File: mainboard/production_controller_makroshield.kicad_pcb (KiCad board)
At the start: 2 copper layers, 165.1 x 202.5 mm, 96 parts, among them J1 CON_TERM_BLK_1X2_TB008A-508-0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, J10 CON_CONNAXIO_MOTOR_DRIVER, J11 CON_CONNAXIO_MOTOR_DRIVER, J12 CON_CONNAXIO_MOTOR_DRIVER, J13 CON_CONNAXIO_MOTOR_DRIVER, J14 CON_CONNAXIO_MOTOR_DRIVER, J15 CON_CONNAXIO_MOTOR_DRIVER, J16 CON_CONNAXIO_MOTOR_DRIVER, J17 CON_CONNAXIO_MOTOR_DRIVER, J18 CON_CONNAXIO_MOTOR_DRIVER, J19 CON_CONNAXIO_MOTOR_DRIVER, J2 CON_TERM_BLK_1X2_TB008A-508-0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, J20 CON_CONNAXIO_MOTOR_DRIVER, J3 CON_HDR_MIKROBUS_ADDON_TH, J4 CON_TERM_BLK_1X2_TB008A-508-0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, J5 CON_HDR_MIKROBUS_SOCKET_TH, J6 CON_CONNAXIO_MOTOR_DRIVER, J7 CON_CONNAXIO_MOTOR_DRIVER, J8 CON_CONNAXIO_MOTOR_DRIVER, J9 CON_CONNAXIO_MOTOR_DRIVER, Q1 TRX_PMOS_AOD4189, Q2 TRX_NPN_MMBT3904-TP, U1 IO_EXP_PI4IOE5V6416ZDEX, U2 IO_EXP_PI4IOE5V6416ZDEX, U3 SUN_CUR_ACS711KEXLT-31AB-T, U4 ADC_NAU7802SGI

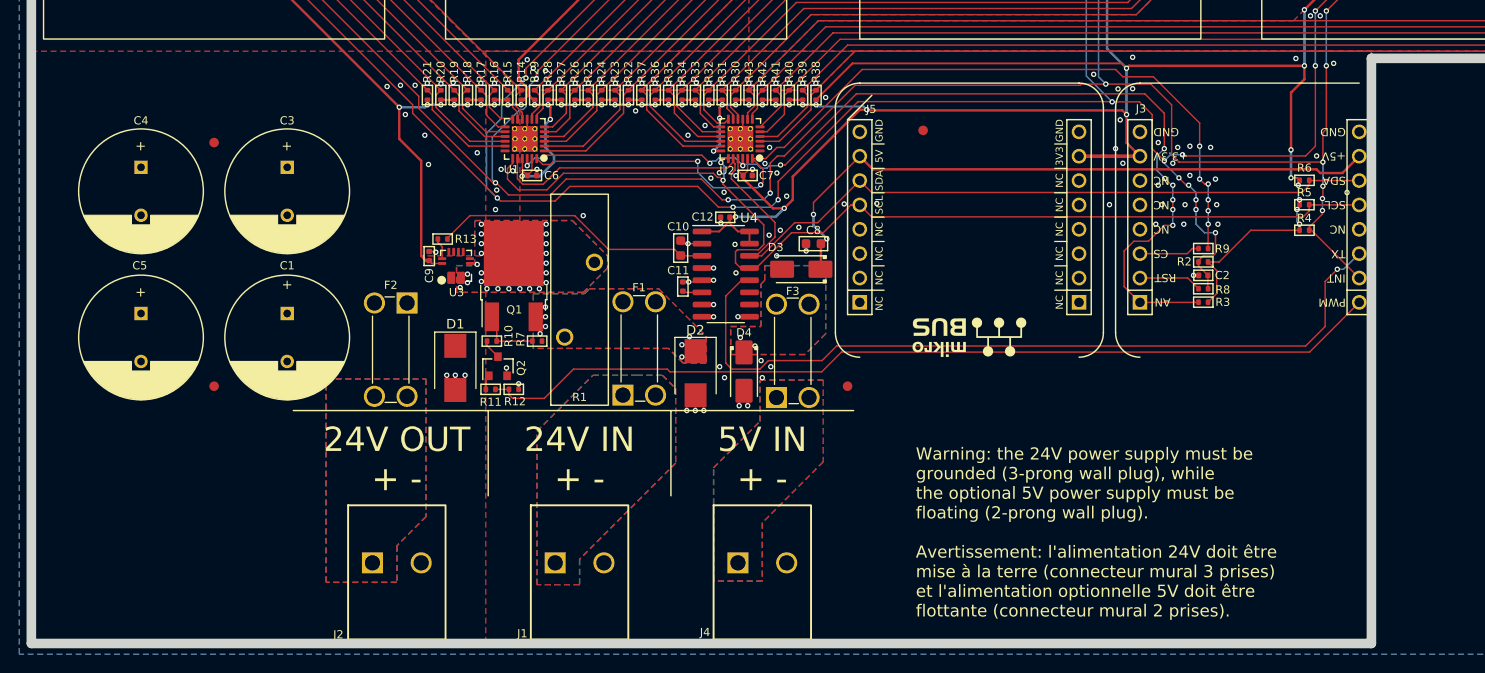
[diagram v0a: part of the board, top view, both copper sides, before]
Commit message: Add LEDs, fix NMOS, Add logos and infos on PCBs.
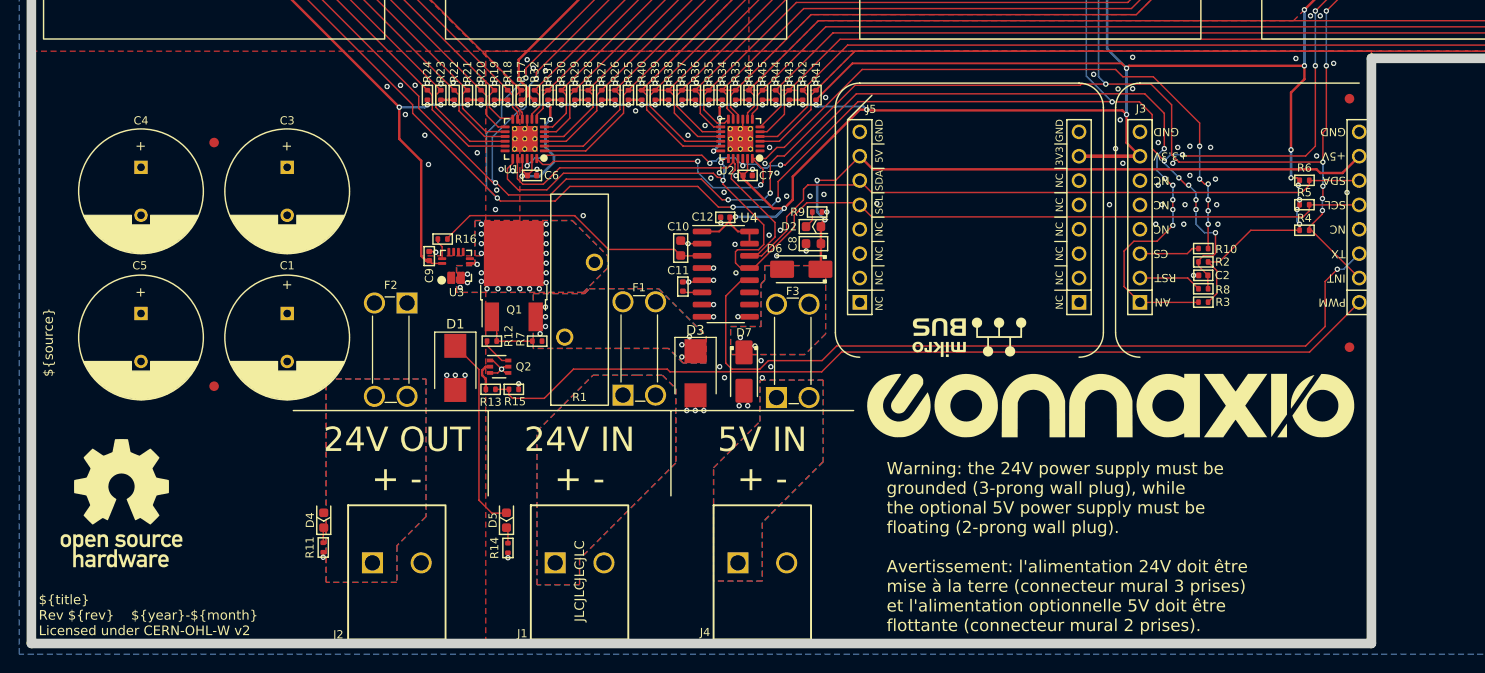
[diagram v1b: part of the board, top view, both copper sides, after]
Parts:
- added D2: DIO_LED_GREEN_150060GS75000, connaxio-diodes:LED_0603_1608M, F.Cu at (159.1, 193.7)
- added D4: DIO_LED_GREEN_150060GS75000, connaxio-diodes:LED_0603_1608M, F.Cu at (108.0, 224.3)
- added D5: DIO_LED_GREEN_150060GS75000, connaxio-diodes:LED_0603_1608M, F.Cu at (127.1, 224.3)
- added G***: LOGO, LOGO, F.Cu at (190.1, 212.4)
- added G***: LOGO, LOGO, F.Cu at (87.0, 222.6)
- added R11: RES_5.10KΩ_1%_0402, connaxio-resistors:RES_0402_1005M, F.Cu at (108.0, 227.2)
- added R14: RES_5.10KΩ_1%_0402, connaxio-resistors:RES_0402_1005M, F.Cu at (127.3, 227.2)
- added R9: RES_1.00KΩ_1%_0402, connaxio-resistors:RES_0402_1005M, F.Cu at (159.5, 192.2)
- Q2: value TRX_NPN_MMBT3904-TP -> TRX_2NPN_BC846S,115; footprint connaxio-sop:SOT-23-3 -> connaxio-sop:SOT-363_SC-70-6
- moved F6 52.5 mm to (215.0, 206.3)
- moved F5 44.6 mm to (215.0, 180.4)
- moved Q2 0.14 mm to (126.3, 208.3), turned to 0 degrees
- renumbered D2 to D3, D3 to D6, D4 to D7, R9 to R10, R10 to R12, R11 to R13, R12 to R15, R13 to R16, R14 to R17, R15 to R18, R16 to R19, R17 to R20, R18 to R21, R19 to R22, R20 to R23, R21 to R24, R22 to R25, R23 to R26, R24 to R27, R25 to R28, R26 to R29, R27 to R30, R28 to R31, R29 to R32, R30 to R33, R31 to R34, R32 to R35, R33 to R36, R34 to R37, R35 to R38, R36 to R39, R37 to R40, R38 to R41, R39 to R42, R40 to R43, R41 to R44, R42 to R45, R43 to R46
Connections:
- Q2 pad 1: Net-(Q2-Pad1) -> GND
- Q2 pad 2: GND -> Net-(R13-Pad2)
- Q2 pad 3: Net-(Q2-Pad3) -> GND
- R12 pad 2: Net-(Q2-Pad3) -> Net-(R12-Pad2)
- R13 pad 2: Net-(Q2-Pad1) -> Net-(R13-Pad2)
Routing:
- net +24VDC: track 0.00 -> 20.6 mm
- net GND: track 24.0 -> 28.8 mm, vias 216 -> 219
- net Net-(R12-Pad2): track 0.00 -> 3.33 mm
- net Net-(R13-Pad2): track 0.00 -> 3.14 mm
- net +5V: track 68.2 -> 70.6 mm
- net Net-(Q2-Pad3): track 2.08 -> 0.00 mm
- net Net-(D2-Pad1): track 0.00 -> 1.80 mm
- net Net-(D5-Pad1): track 0.00 -> 1.65 mm
- net Net-(D4-Pad1): track 0.00 -> 1.59 mm
- net Net-(Q2-Pad1): track 1.54 -> 0.00 mm
- net /I2C_SDA: track 107.2 -> 108.7 mm
- net /I2C_SCL: track 111.6 -> 112.5 mm
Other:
- board text added: "${source}"
- board text added: "${title} Rev ${rev} ${year}-${month} Licensed under CERN-OHL-W v2"
- board text added: "JLCJLCJLCJLC"

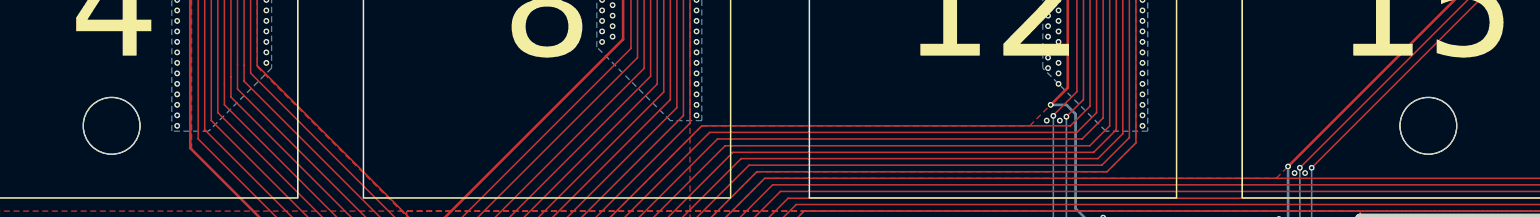
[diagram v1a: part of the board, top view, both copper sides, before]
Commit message: Add Enclosure piercing guide and fix h-bridge-driver NMOS pads.
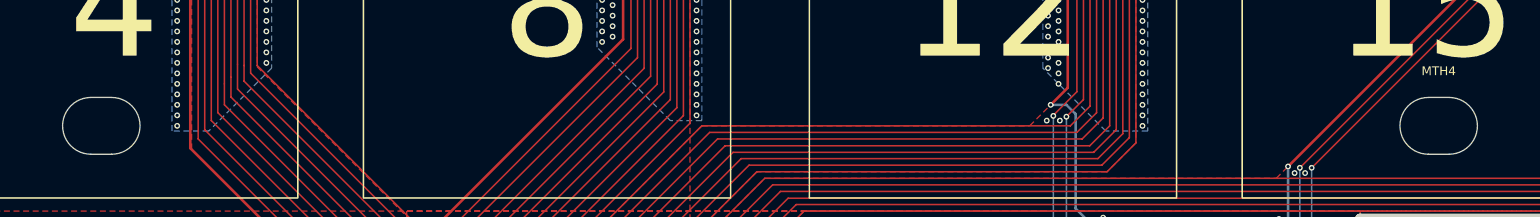
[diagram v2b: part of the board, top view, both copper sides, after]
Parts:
- MTH3, MTH4: value MTH_M5_NPTH -> MTH_SLOT_M5_2MM_NPTH; footprint connaxio-mechanical:MTH_M5_NPTH -> connaxio-mechanical:MTH_SLOT_M5_2MM_NPTH
- moved MTH4 170.8 mm to (224.9, 167.2)
- moved MTH2 170.0 mm to (223.9, 54.7)
- moved MTH3 128.5 mm to (95.4, 167.2)
- moved MTH1 127.5 mm to (96.4, 54.7)

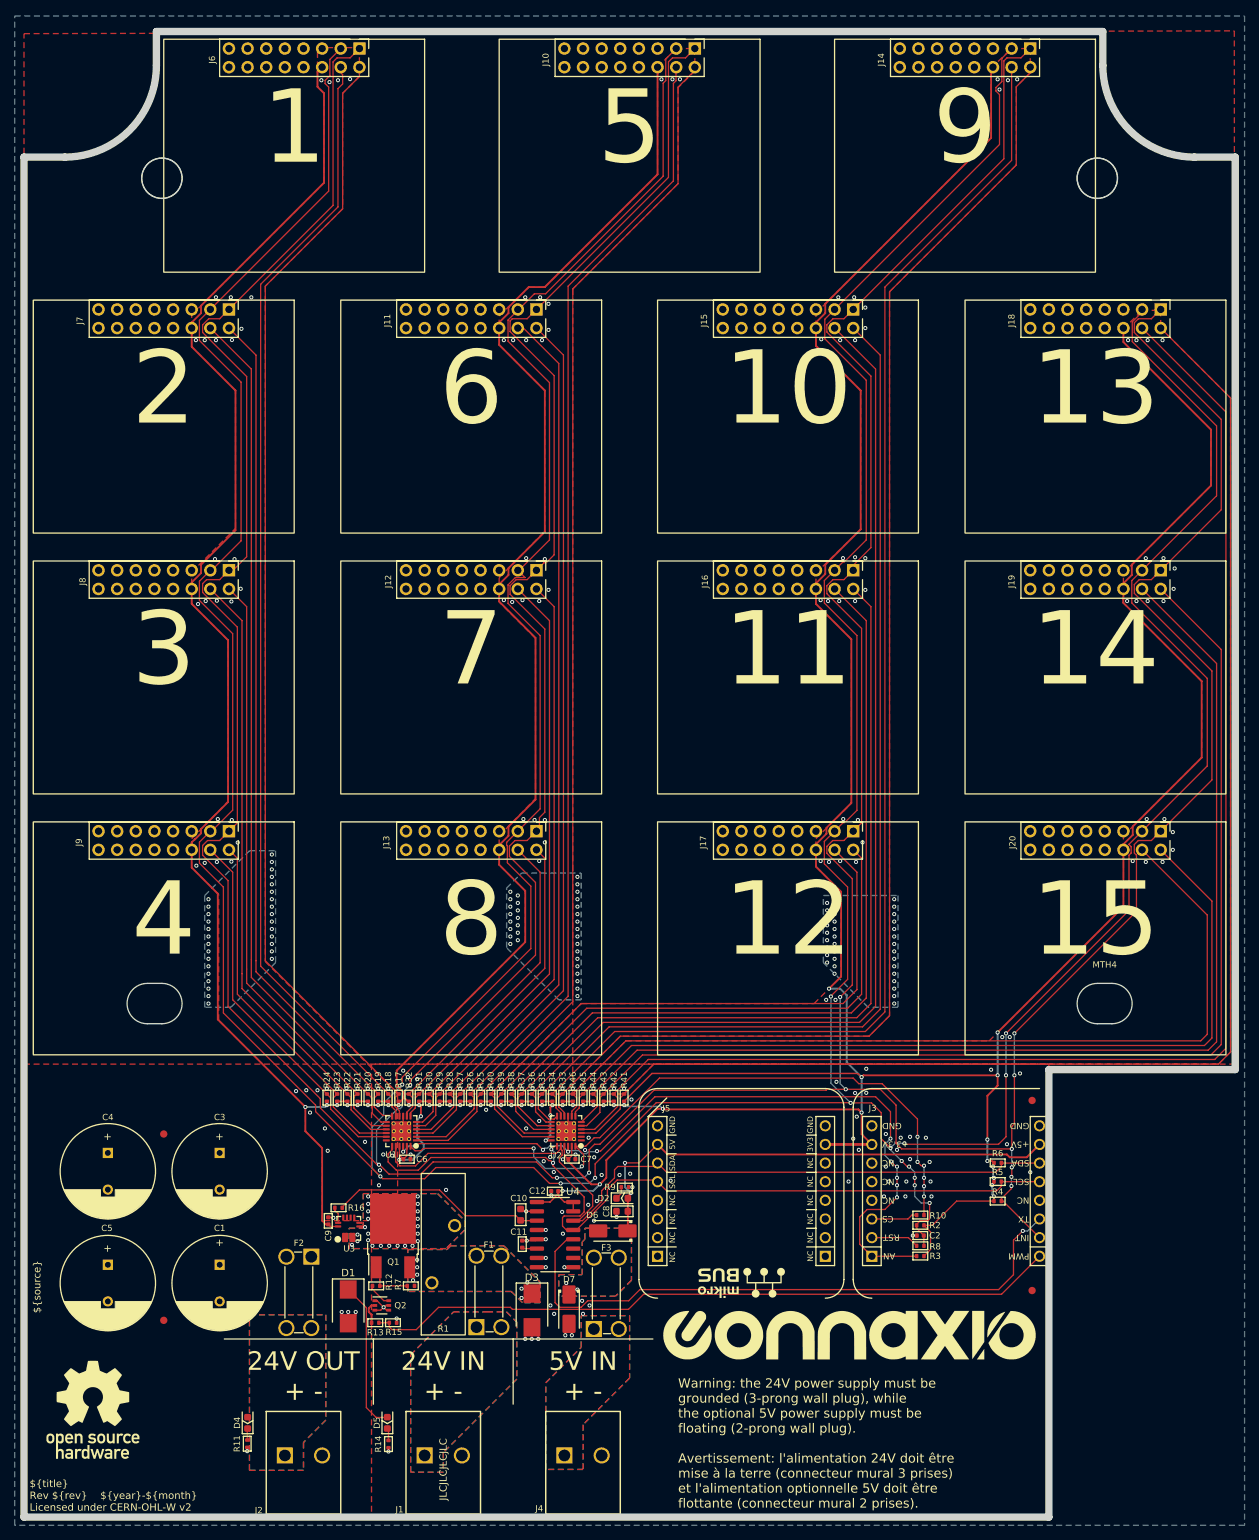
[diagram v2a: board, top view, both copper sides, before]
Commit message: Invert connectors (male/female) Replace TH connectors with SMD ones on mainboard Add 555 timer on simple-switch to generate 60 Hz Add jumper on simple-switch to select AC Add series I2C resistors on mainboard from mikroBUS socket
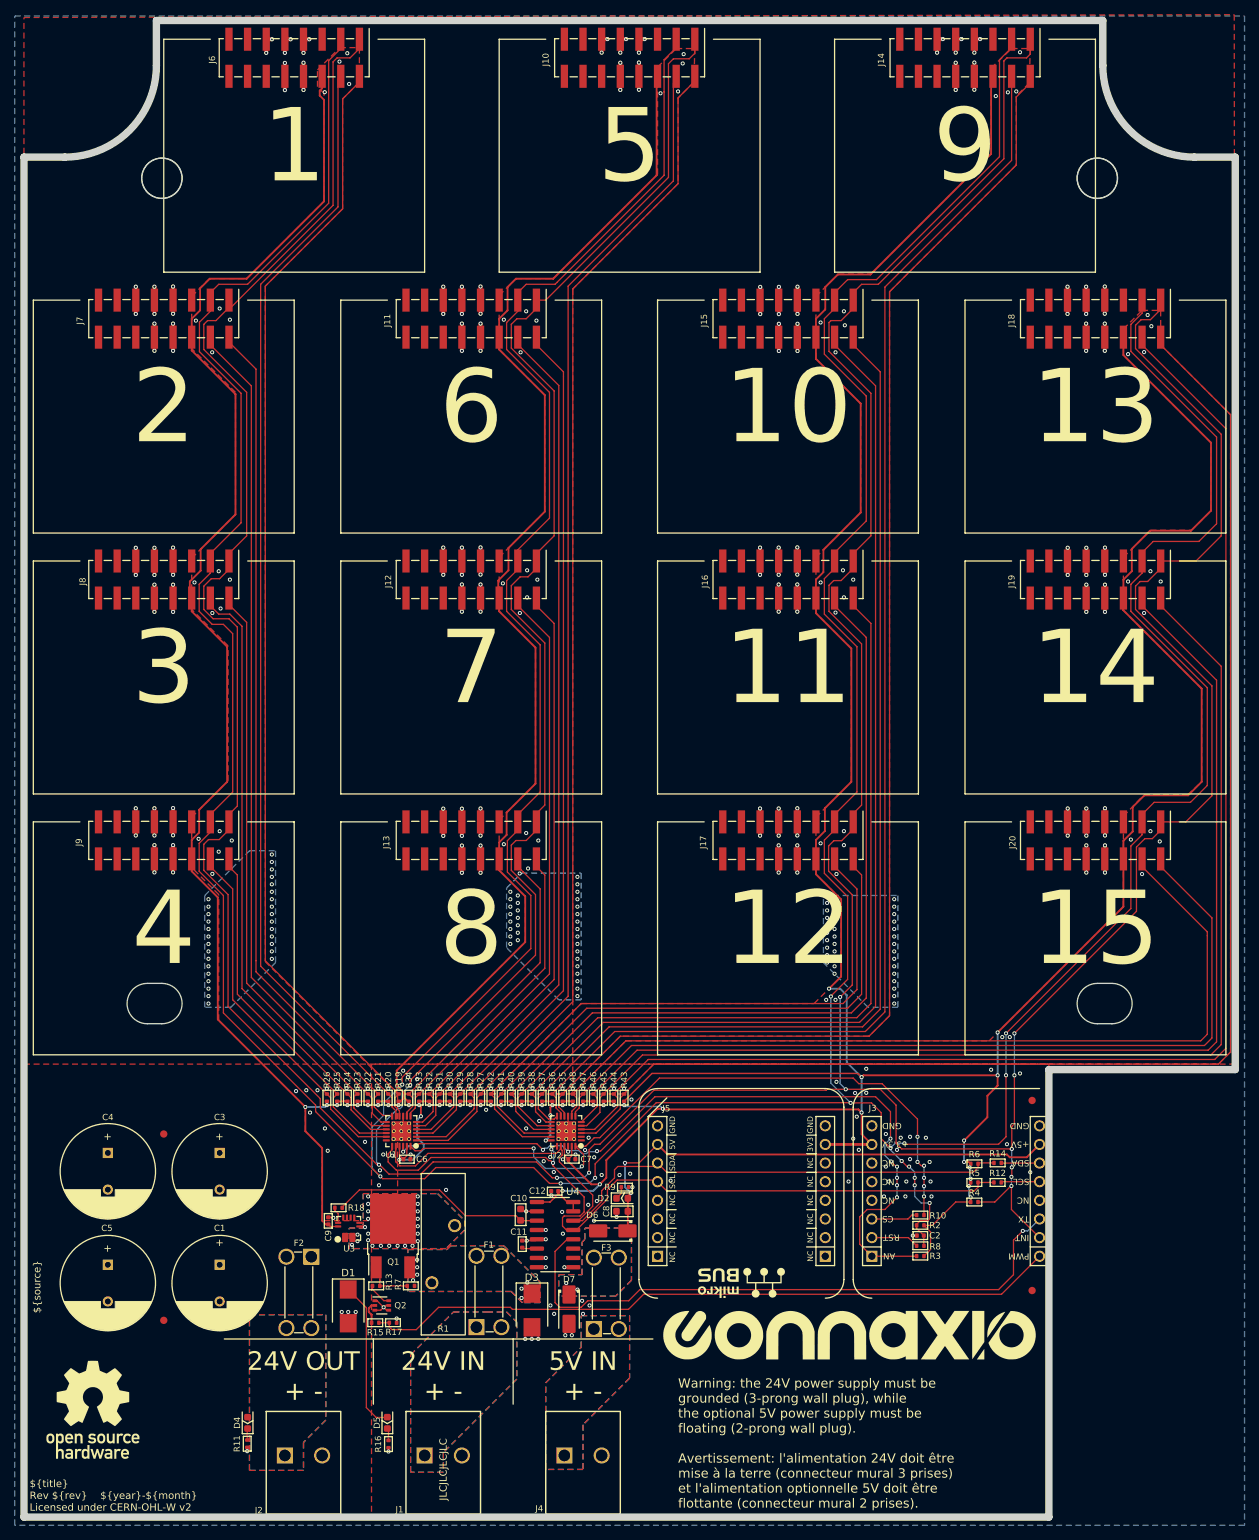
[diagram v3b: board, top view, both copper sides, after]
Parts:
- added R12: RES_226Ω_1%_0402, connaxio-resistors:RES_0402_1005M, F.Cu at (210.3, 191.6)
- added R14: RES_226Ω_1%_0402, connaxio-resistors:RES_0402_1005M, F.Cu at (210.3, 188.9)
- moved R6 3.18 mm to (207.1, 189.0)
- moved R4 3.18 mm to (207.1, 194.2)
- moved R5 3.18 mm to (207.1, 191.6)
- renumbered R12 to R13, R13 to R15, R14 to R16, R15 to R17, R16 to R18, R17 to R19, R18 to R20, R19 to R21, R20 to R22, R21 to R23, R22 to R24, R23 to R25, R24 to R26, R25 to R27, R26 to R28, R27 to R29, R28 to R30, R29 to R31, R30 to R32, R31 to R33, R32 to R34, R33 to R35, R34 to R36, R35 to R37, R36 to R38, R37 to R39, R38 to R40, R39 to R41, R40 to R42, R41 to R43, R42 to R44, R43 to R45, R44 to R46, R45 to R47, R46 to R48
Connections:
- J3 pad 13: /I2C_SCL -> Net-(J3-Pad13)
- J3 pad 14: /I2C_SDA -> Net-(J3-Pad14)
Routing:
- net GND: track 28.8 -> 297.4 mm, vias 219 -> 340
- net RST_MOT: track 787.6 -> 803.4 mm
- net FAULT: track 800.5 -> 814.1 mm
- net /I2C_SDA: track 108.7 -> 102.3 mm
- net /I2C_SCL: track 112.5 -> 106.2 mm
- net Net-(J3-Pad13): track 0.00 -> 5.19 mm
- net Net-(J3-Pad14): track 0.00 -> 5.18 mm
- net +3.3V: track 898.3 -> 902.7 mm
- net CTRLB5: track 163.2 -> 160.9 mm
- net CTRLB1: track 155.7 -> 153.4 mm
- net CTRLB11: track 119.8 -> 117.5 mm
- net CTRLB10: track 151.9 -> 149.6 mm
- net CTRLA15: track 120.9 -> 118.6 mm
- net CTRLA13: track 196.6 -> 194.3 mm
- net CTRLB14: track 158.8 -> 156.5 mm
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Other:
- board size 165.1 x 202.5 mm -> 165.1 x 204 mm
